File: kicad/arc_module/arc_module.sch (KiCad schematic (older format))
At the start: 20 parts

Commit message: restructure & add ARC
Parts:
- removed L?: L_Small, symbol L_Small
- added D3: BAS16H, Diodes_SMD:D_SOD-323_HandSoldering, symbol D_Small
- added J1: CONN_01X07, Pin_Headers:Pin_Header_Straight_1x07_Pitch2.54mm, symbol CONN_01X07
- added J10, J11, J9: CONN_01X03, Pin_Headers:Pin_Header_Straight_1x03_Pitch2.54mm, symbol CONN_01X03
- added J2: CONN_01X02, Pin_Headers:Pin_Header_Straight_1x02_Pitch2.54mm, symbol CONN_01X02
- added L1: 300ohm @ 100MHz, Inductors_SMD:L_0805_HandSoldering, symbol Ferrite_Bead_Small
- added P5, P6: CONN_01X01, Pin_Headers:Pin_Header_Straight_1x01_Pitch2.54mm, symbol CONN_01X01
- added R10, R13, R14: 10k, Resistors_SMD:R_0805_HandSoldering, symbol R
- C4, C5, C6, C7: renamed from C?; footprint (none) -> Capacitors_SMD:C_0805_HandSoldering
- C8: renamed from C?; footprint (none) -> Capacitors_THT:CP_Radial_D5.0mm_P2.00mm
- P3: renamed from P?; footprint (none) -> Pin_Headers:Pin_Header_Straight_1x02_Pitch2.54mm
- P4: renamed from P?; footprint (none) -> Pin_Headers:Pin_Header_Straight_1x01_Pitch2.54mm
- R11, R12, R2, R3, R4, R5, R6, R8, R9: renamed from R?; footprint (none) -> Resistors_SMD:R_0805_HandSoldering
- R7: renamed from R?; value 11k -> 39k; footprint (none) -> Resistors_SMD:R_0805_HandSoldering
- U3: renamed from U?; footprint (none) -> Housings_SOIC:SOIC-14_3.9x8.7mm_Pitch1.27mm
- gave numbers to parts that had none: 1
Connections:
- net +3V3: now also J10.1 (P1), J9.1 (P1), L1.1
- net +5V: now also J1.6 (P6)
- net CEC: now also J1.1 (P1)
- net GND: now also J1.5 (P5), J10.3 (P3), J11.3 (P3), J9.3 (P3), R10.1, R13.1, R14.1; no longer U3.1 (ARC_TX_EN)
- net HDMI_SCL: now also J1.3 (P3)
- net HDMI_SDA: now also J1.4 (P4)
- net HEAC+: now also J1.2 (P2)
- net HEAC-: now also D3.2 (A), J1.7 (P7)
- net Module Common/I2S1_mod: now also R10.2
- net Module Common/I2S2_mod: now also R13.2
- net Module Common/I2S3_mod: now also R14.2
- net Module Common/SCL: now also J2.2 (P2)
- net Module Common/SDA: now also J2.1 (P1)
- net VDDA: now also L1.2; no longer U3.14 (ARC_RX_EN)
- net SPD_Tx: now reaches R9.1, U3.12 (SPDIF_IN)
- net SPD_Tx: now also J11.2 (P2)
- net SPD_Rx: now reaches U3.13 (SPDIF_OUT)
- net SPD_Rx: now also J11.1 (P1)
- new net HDMI_HotPlug: D3.1 (K), P6.1 (P1)
- new net Rx_En: J10.2 (P2), U3.14 (ARC_RX_EN)
- new net Tx_En: J9.2 (P2), U3.1 (ARC_TX_EN)
- new net arc tx/Ctrl_Tx: P5.1 (P1)
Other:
- note added: "11k for Tx"
- note added: "Change CS8416 jumpers to SMD solder bridges?"
- note added: "Check packages for:\nInductors\nBig Caps\nCS8416\nEP91H0"
- note added: "For HDMI breakout, pins 13-19"
- note added: "Not sure how to drive this yet."
- note removed: "check spec"
- moved on the sheet: C4, C5, C6, C7, C8, P3, P4, R11, R12, R2, R3, R4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

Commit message: draft layout
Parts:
- added P7, P8: CONN_01X01, Pin_Headers:Pin_Header_Straight_1x01_Pitch2.54mm, symbol CONN_01X01
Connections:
- net Module Common/IO0: now also P7.1 (P1), P8.1 (P1)
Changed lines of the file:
@@
 Text Label 1350 5850 2    60   ~ 0
 HDMI_HotPlug
+$Comp
+L CONN_01X01 P7
+U 1 1 58FC7DA1
+P 10950 4900
+F 0 "P7" H 10950 5000 50  0000 C CNN
+F 1 "CONN_01X01" V 11050 4900 50  0000 C CNN
+F 2 "Pin_Headers:Pin_Header_Straight_1x01_Pitch2.54mm" H 10950 4900 50  0001 C CNN
+F 3 "" H 10950 4900 50  0000 C CNN
+	1    10950 4900
+	1    0    0    -1
+$EndComp
+$Comp
+L CONN_01X01 P8
+U 1 1 58FC7F85
+P 10950 5400
+F 0 "P8" H 10950 5500 50  0000 C CNN
+F 1 "CONN_01X01" V 11050 5400 50  0000 C CNN
+F 2 "Pin_Headers:Pin_Header_Straight_1x01_Pitch2.54mm" H 10950 5400 50  0001 C CNN
+F 3 "" H 10950 5400 50  0000 C CNN
+	1    10950 5400
+	1    0    0    -1
+$EndComp
+Wire Wire Line
+	10500 5100 10750 5100
+Wire Wire Line
+	10750 4900 10750 5400
+Connection ~ 10750 5100
 $EndSCHEMATC

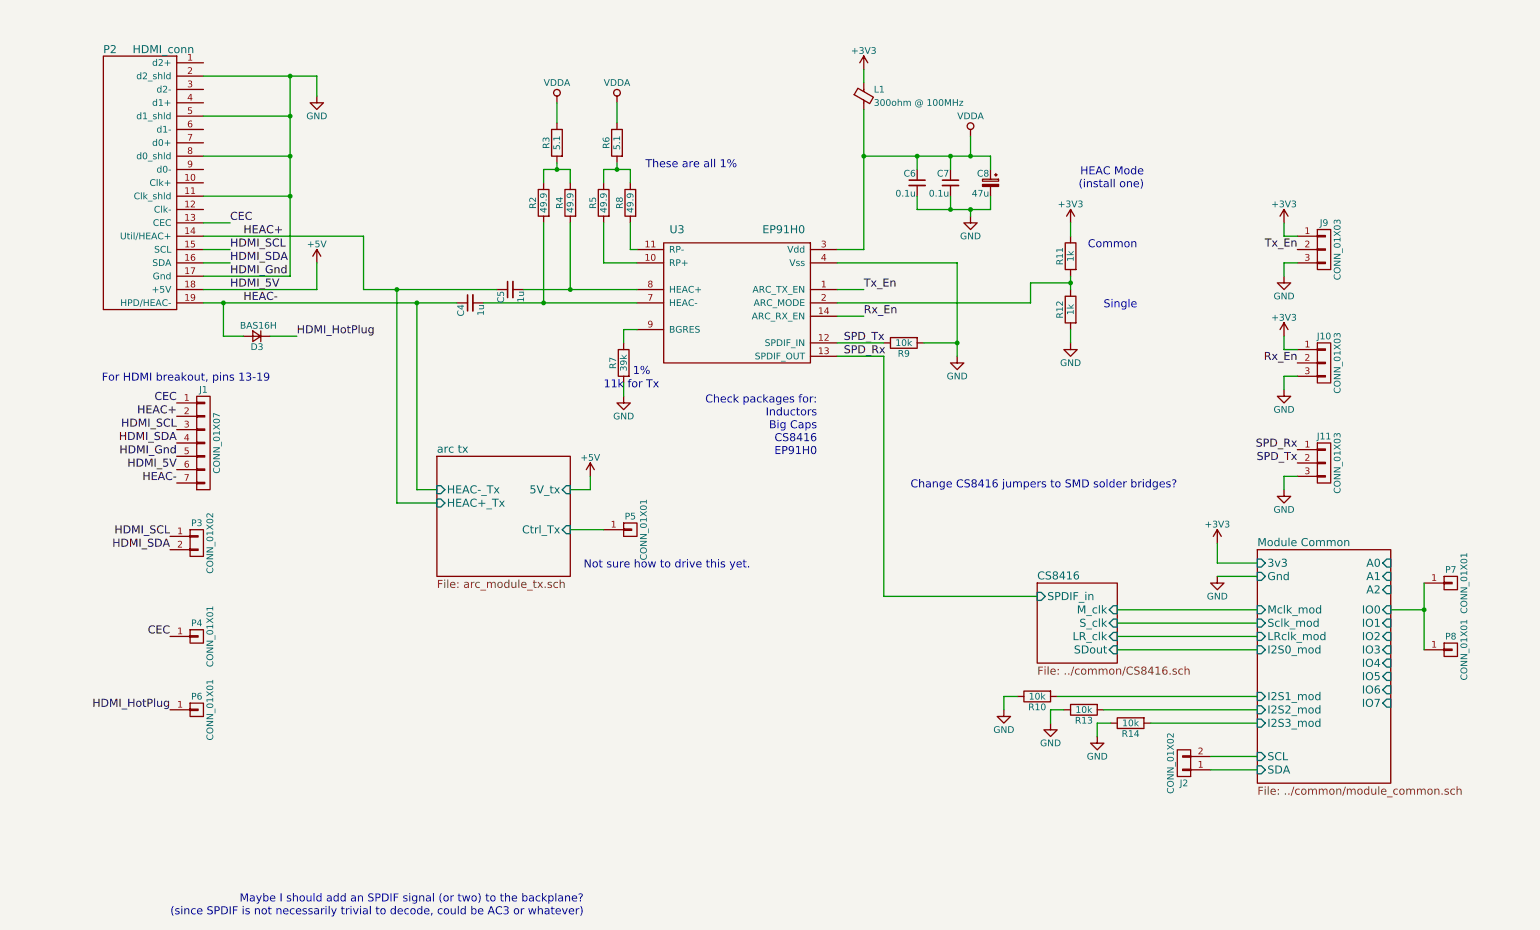
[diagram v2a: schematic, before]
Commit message: silkscreen & test points
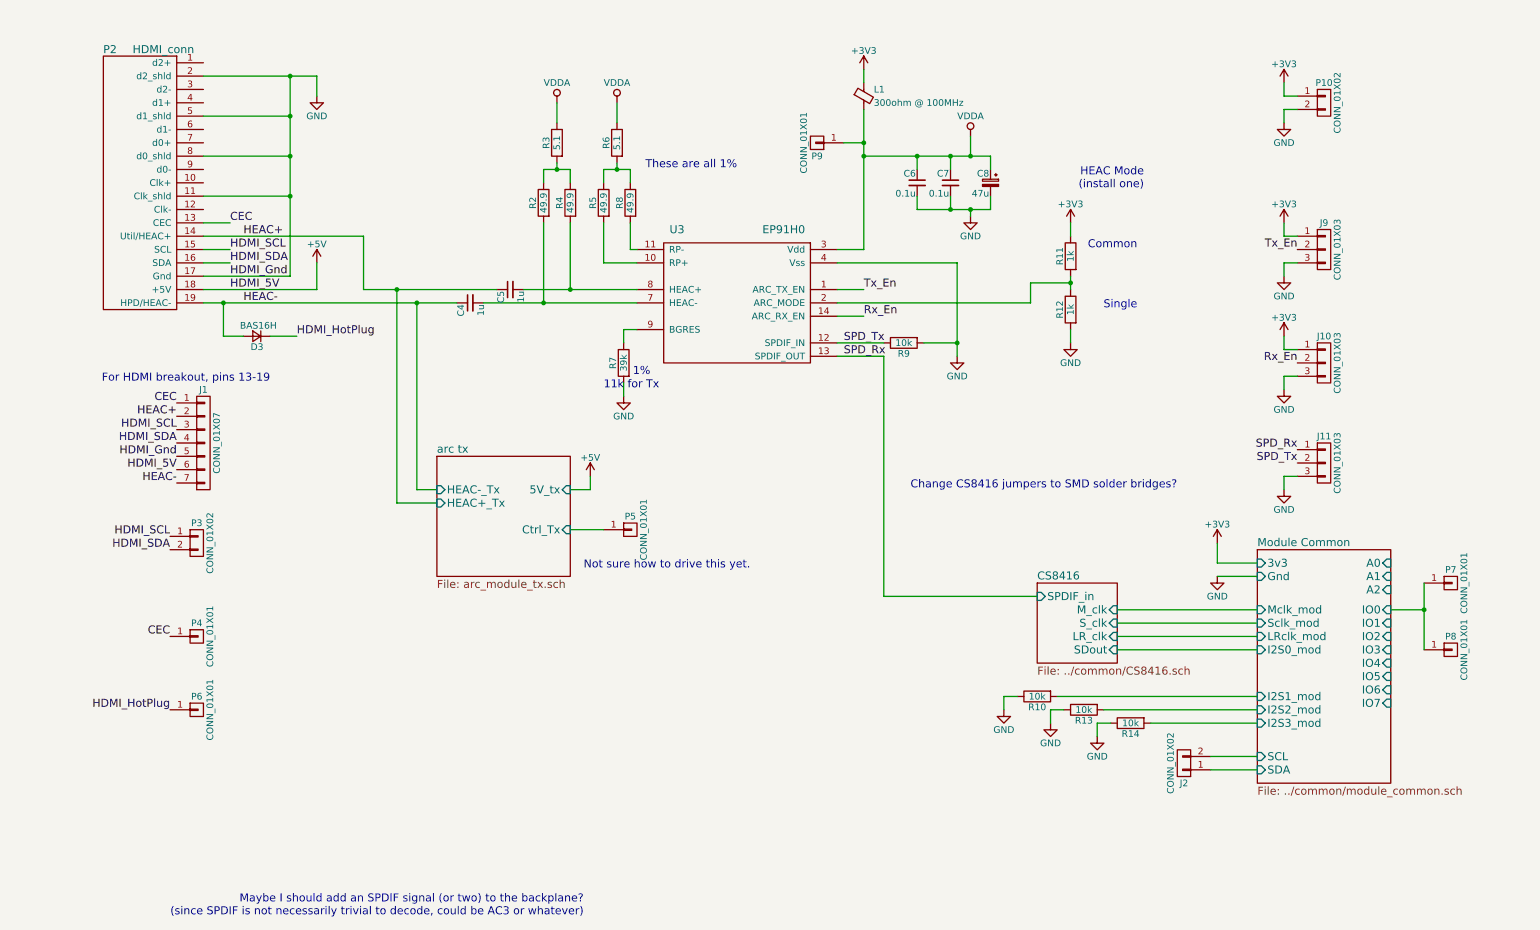
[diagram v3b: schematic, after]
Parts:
- added P10: CONN_01X02, Pin_Headers:Pin_Header_Straight_1x02_Pitch2.54mm, symbol CONN_01X02
- added P9: CONN_01X01, Pin_Headers:Pin_Header_Straight_1x01_Pitch2.54mm, symbol CONN_01X01
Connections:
- net +3V3: now also P10.1 (P1)
- net GND: now also P10.2 (P2)
- net VDDA: now also P9.1 (P1)
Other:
- note removed: "Check packages for:\nInductors\nBig Caps\nCS8416\nEP91H0"
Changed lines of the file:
@@
 	8100 2200 8100 2300
 Wire Wire Line
-	8100 2600 8100 2700
+	8100 2600 8100 2650
+Wire Wire Line
+	8100 2650 8100 2700
 Wire Wire Line
 	8100 3000 8100 3100
@@
 	7250 3100 7000 3100
 Wire Wire Line
-	7250 2500 7250 3200
+	7250 2500 7250 3100
+Wire Wire Line
+	7250 3100 7250 3200
 Wire Wire Line
 	4850 3000 4750 3000
@@
 	4700 1750 4700 1800
 Wire Wire Line
-	4600 1800 4800 1800
+	4600 1800 4700 1800
+Wire Wire Line
+	4700 1800 4800 1800
 Wire Wire Line
 	4800 1800 4800 1900
@@
 	4250 1750 4250 1800
 Wire Wire Line
-	4150 1800 4350 1800
+	4150 1800 4250 1800
+Wire Wire Line
+	4250 1800 4350 1800
 Wire Wire Line
 	4350 1800 4350 1900
@@
 	4250 1300 4250 1450
 Wire Wire Line
-	2800 2700 3800 2700
-Wire Wire Line
-	6550 1700 7500 1700
+	2800 2700 3050 2700
+Wire Wire Line
+	3050 2700 3800 2700
+Wire Wire Line
+	6550 1700 6950 1700
+Wire Wire Line
+	6950 1700 7200 1700
+Wire Wire Line
+	7200 1700 7350 1700
+Wire Wire Line
+	7350 1700 7500 1700
 Wire Wire Line
 	7500 1700 7500 1800
@@
 	7500 2100 7500 2000
 Wire Wire Line
-	6950 2100 7500 2100
+	6950 2100 7200 2100
+Wire Wire Line
+	7200 2100 7350 2100
+Wire Wire Line
+	7350 2100 7500 2100
 Wire Wire Line
 	7350 2100 7350 2150
@@
 	9200 4850 9500 4850
 Wire Wire Line
-	1600 1100 2450 1100
+	1600 1100 2250 1100
+Wire Wire Line
+	2250 1100 2450 1100
 Wire Wire Line
 	2450 1100 2450 1250
@@
 	1600 1400 2250 1400
 Wire Wire Line
-	2250 1100 2250 2600
+	2250 1100 2250 1400
+Wire Wire Line
+	2250 1400 2250 1700
+Wire Wire Line
+	2250 1700 2250 2000
+Wire Wire Line
+	2250 2000 2250 2600
 Connection ~ 2250 1100
 Wire Wire Line
@@
 	4850 2500 4600 2500
 Wire Wire Line
-	4000 2700 4850 2700
-Wire Wire Line
-	3700 2800 4850 2800
+	4000 2700 4350 2700
+Wire Wire Line
+	4350 2700 4850 2700
+Wire Wire Line
+	3700 2800 4150 2800
+Wire Wire Line
+	4150 2800 4850 2800
 Connection ~ 4350 2700
 Connection ~ 4150 2800
@@
 	2800 2300 2800 2700
 Wire Wire Line
-	1600 2800 3500 2800
+	1600 2800 1750 2800
+Wire Wire Line
+	1750 2800 3200 2800
+Wire Wire Line
+	3200 2800 3500 2800
 $Comp
 L R R10
@@
 Text Notes 2100 3400 2    60   ~ 0
 For HDMI breakout, pins 13-19
-Text Notes 6200 3950 2    60   ~ 0
-Check packages for:\nInductors\nBig Caps\nCS8416\nEP91H0
 Text Notes 6900 4200 0    60   ~ 0
 Change CS8416 jumpers to SMD solder bridges?
@@
 SPD_Rx
 Wire Wire Line
-	6550 1350 6550 2400
+	6550 1350 6550 1600
+Wire Wire Line
+	6550 1600 6550 1700
+Wire Wire Line
+	6550 1700 6550 2400
 Wire Wire Line
 	6550 2400 6350 2400
@@
 	10500 5100 10750 5100
 Wire Wire Line
-	10750 4900 10750 5400
+	10750 4900 10750 5100
+Wire Wire Line
+	10750 5100 10750 5400
 Connection ~ 10750 5100
+$Comp
+L CONN_01X02 P10
+U 1 1 58FC9BF1
+P 10000 1300
+F 0 "P10" H 10000 1450 50  0000 C CNN
+F 1 "CONN_01X02" V 10100 1300 50  0000 C CNN
+F 2 "Pin_Headers:Pin_Header_Straight_1x02_Pitch2.54mm" H 10000 1300 50  0001 C CNN
+F 3 "" H 10000 1300 50  0000 C CNN
+	1    10000 1300
+	1    0    0    -1
+$EndComp
+$Comp
+L +3V3 #PWR023
+U 1 1 58FCA199
+P 9700 1150
+F 0 "#PWR023" H 9700 1000 50  0001 C CNN
+F 1 "+3V3" H 9700 1290 50  0000 C CNN
+F 2 "" H 9700 1150 50  0000 C CNN
+F 3 "" H 9700 1150 50  0000 C CNN
+	1    9700 1150
+	-1   0    0    -1
+$EndComp
+Wire Wire Line
+	9700 1150 9700 1250
+Wire Wire Line
+	9700 1250 9800 1250
+$Comp
+L GND #PWR024
+U 1 1 58FCA4C0
+P 9700 1450
+F 0 "#PWR024" H 9700 1200 50  0001 C CNN
+F 1 "GND" H 9700 1300 50  0000 C CNN
+F 2 "" H 9700 1450 50  0000 C CNN
+F 3 "" H 9700 1450 50  0000 C CNN
+	1    9700 1450
+	-1   0    0    -1
+$EndComp
+Wire Wire Line
+	9800 1350 9700 1350
+Wire Wire Line
+	9700 1350 9700 1450
+$Comp
+L CONN_01X01 P9
+U 1 1 58FCACA6
+P 6200 1600
+F 0 "P9" H 6200 1700 50  0000 C CNN
+F 1 "CONN_01X01" V 6300 1600 50  0000 C CNN
+F 2 "Pin_Headers:Pin_Header_Straight_1x01_Pitch2.54mm" H 6200 1600 50  0001 C CNN
+F 3 "" H 6200 1600 50  0000 C CNN
+	1    6200 1600
+	-1   0    0    1
+$EndComp
+Wire Wire Line
+	6400 1600 6550 1600
+Connection ~ 6550 1600
 $EndSCHEMATC
